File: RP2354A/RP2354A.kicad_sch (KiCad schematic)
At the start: 22 parts, among them J101 USB4085-GF-A, J102 AudioJack2_SwitchT, J103 AudioJack2_SwitchT, Q101 MMBF5103

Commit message: First cut at BOM selection for caps and resistors
The size choices were a bit random, this standardizes on 0402 for
resistors.  Also, optimize the BOM by just sharing values where they
don't matter that much.

For example, we need those 5k1 resistors for the USB CC pulldowns, and
we might as well then use that for the i2c pullup resistors too.  And
the self-biasing source resistor for the JFET input could use the same.

For similar reasons, just standardize on 33R for the low value resistors
that we use for the USB data line serial termination and the analog
voltage RC filtering.

Capacitors are 0402 for small values (0.1uF and smaller) or 0603 for
bigger capacitance values.  That seems to match availability.

Signed-off-by: Linus Torvalds <torvalds@linux-foundation.org>
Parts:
- C101, C103, C105, C106, C107: footprint Capacitor_SMD:C_1206_3216Metric -> Capacitor_SMD:C_0603_1608Metric
- C102, C104: footprint Capacitor_SMD:C_0805_2012Metric -> Capacitor_SMD:C_0402_1005Metric
- R106, R107: value 3k3 -> 5k1
- R110: value 100R -> 33R
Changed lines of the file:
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@@
 			)
 		)
-		(property "Footprint" "Capacitor_SMD:C_1206_3216Metric"
+		(property "Footprint" "Capacitor_SMD:C_0603_1608Metric"
 			(at 43.18 118.4148 0)
 			(effects
@@
 			)
 		)
-		(property "Footprint" "Capacitor_SMD:C_0805_2012Metric"
+		(property "Footprint" "Capacitor_SMD:C_0402_1005Metric"
 			(at 154.6352 99.06 0)
 			(effects
@@
 			)
 		)
-		(property "Footprint" "Capacitor_SMD:C_0805_2012Metric"
+		(property "Footprint" "Capacitor_SMD:C_0402_1005Metric"
 			(at 58.7248 130.81 0)
 			(effects
@@
 			)
 		)
-		(property "Footprint" "Capacitor_SMD:C_1206_3216Metric"
+		(property "Footprint" "Capacitor_SMD:C_0603_1608Metric"
 			(at 165.4048 41.91 0)
 			(effects
@@
 			)
 		)
-		(property "Value" "100R"
+		(property "Value" "33R"
 			(at 176.53 34.29 90)
 			(effects
@@
 			)
 		)
-		(property "Value" "3k3"
+		(property "Value" "5k1"
 			(at 83.82 132.08 0)
 			(effects
@@
 			)
 		)
-		(property "Footprint" "Capacitor_SMD:C_1206_3216Metric"
+		(property "Footprint" "Capacitor_SMD:C_0603_1608Metric"
 			(at 100.33 125.4252 0)
 			(effects
@@
 			)
 		)
-		(property "Footprint" "Capacitor_SMD:C_1206_3216Metric"
+		(property "Footprint" "Capacitor_SMD:C_0603_1608Metric"
 			(at 167.64 93.0148 0)
 			(effects
@@
 			)
 		)
-		(property "Value" "3k3"
+		(property "Value" "5k1"
 			(at 88.9 43.18 0)
 			(effects
@@
 			)
 		)
-		(property "Footprint" "Capacitor_SMD:C_1206_3216Metric"
+		(property "Footprint" "Capacitor_SMD:C_0603_1608Metric"
 			(at 185.7248 41.91 0)
 			(effects

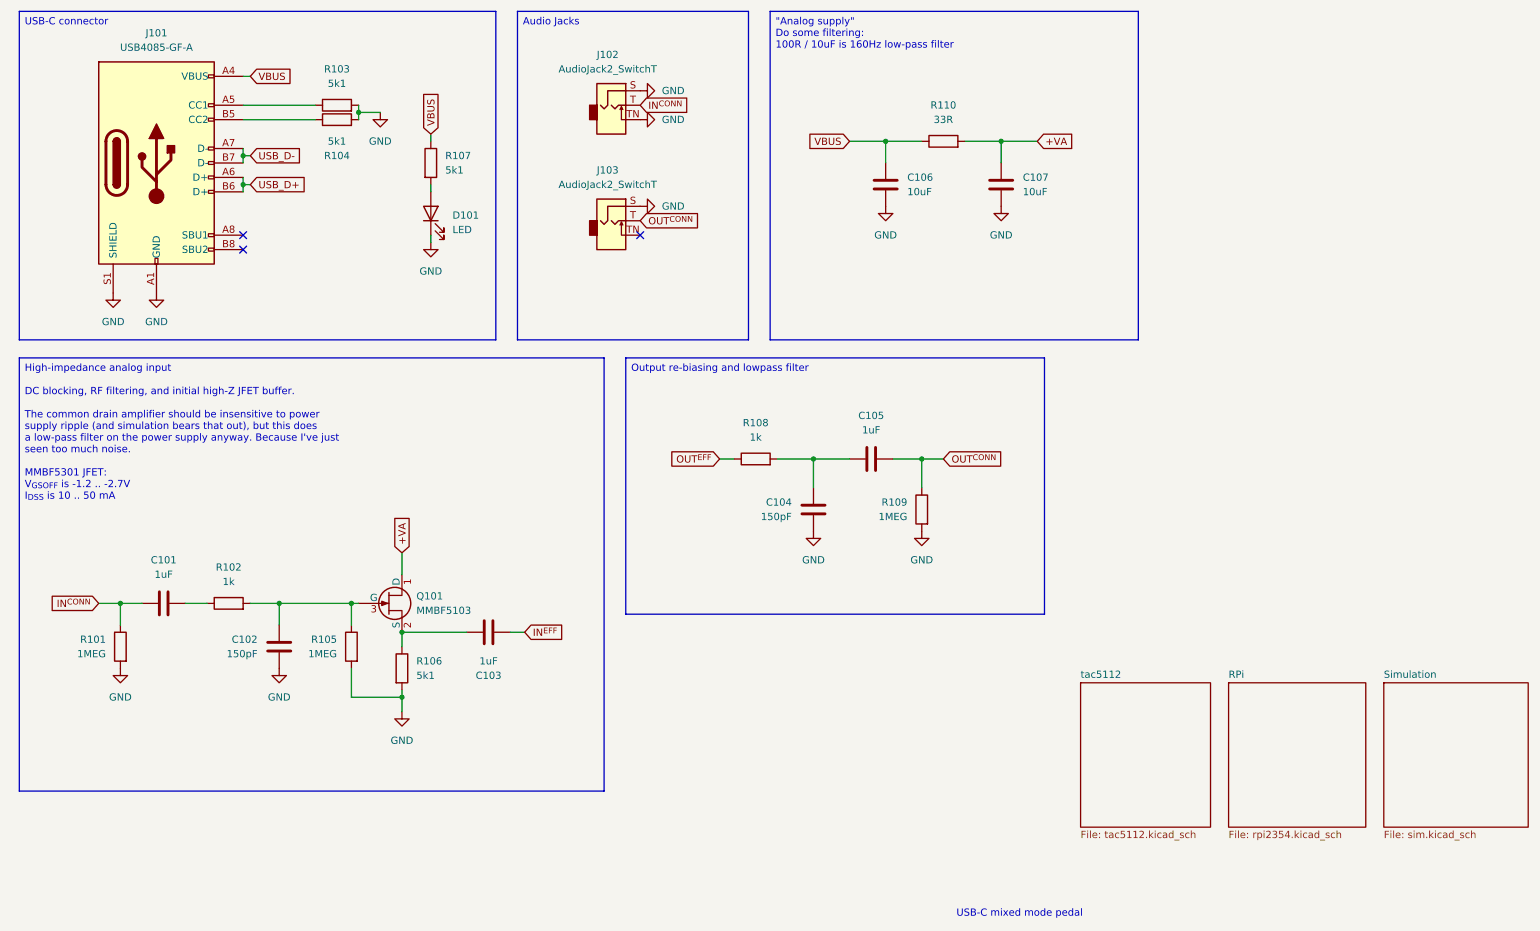
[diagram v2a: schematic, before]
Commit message: Switch the MMBF5103 JFET over to a OPA365 op amp
This is a long time coming, but it was triggered by jlcpcb not stocking
the MMBF5103, and all the alternatives looked worse.  So I guess sanity
has to prevail, and I should use an opamp rather than a discrete JFET
input stage.

I looked at the J201 - which I have tested and works, but has a
potentially very low V_{GSOFF} that will cause clipping.  And the
MMBFJ309L looked good in simulation and had better parameter values, but
I've never tested it, so it seemed a bit risky particularly since the
intended market seems to be for much higher frequency circuits.

I even looked at the JFE150, which is another silly-expensive thing sold
to audio markets.  I guess that tracks.

In the end, a plain simple opamp is definitely the sane choice.

To rebias the incoming signal, this uses the MICBIAS from the TAC5112,
which is typically 2.75V (but can be programmed to 2.5V or turned off
entirely etc).  It's there, it's almost what it is meant for, so let's
use it.

The OPA365 looks fine, and does rail-to-rail input and output and can do
single supplies down to 2.2V, but rather than put even more on the 3.3V
rail (and limiting the voltage swing), this just uses the 5V USB VBUS
power supply.

This does have some minimal caps for filtering (replacing the old +VA
supply to the JFET) but the OPA365 also claims good PSRR.

This all does seem like the right thing to do, but I'm still a bit sad
since the discrete JFET was just more interesting.

Signed-off-by: Linus Torvalds <torvalds@linux-foundation.org>
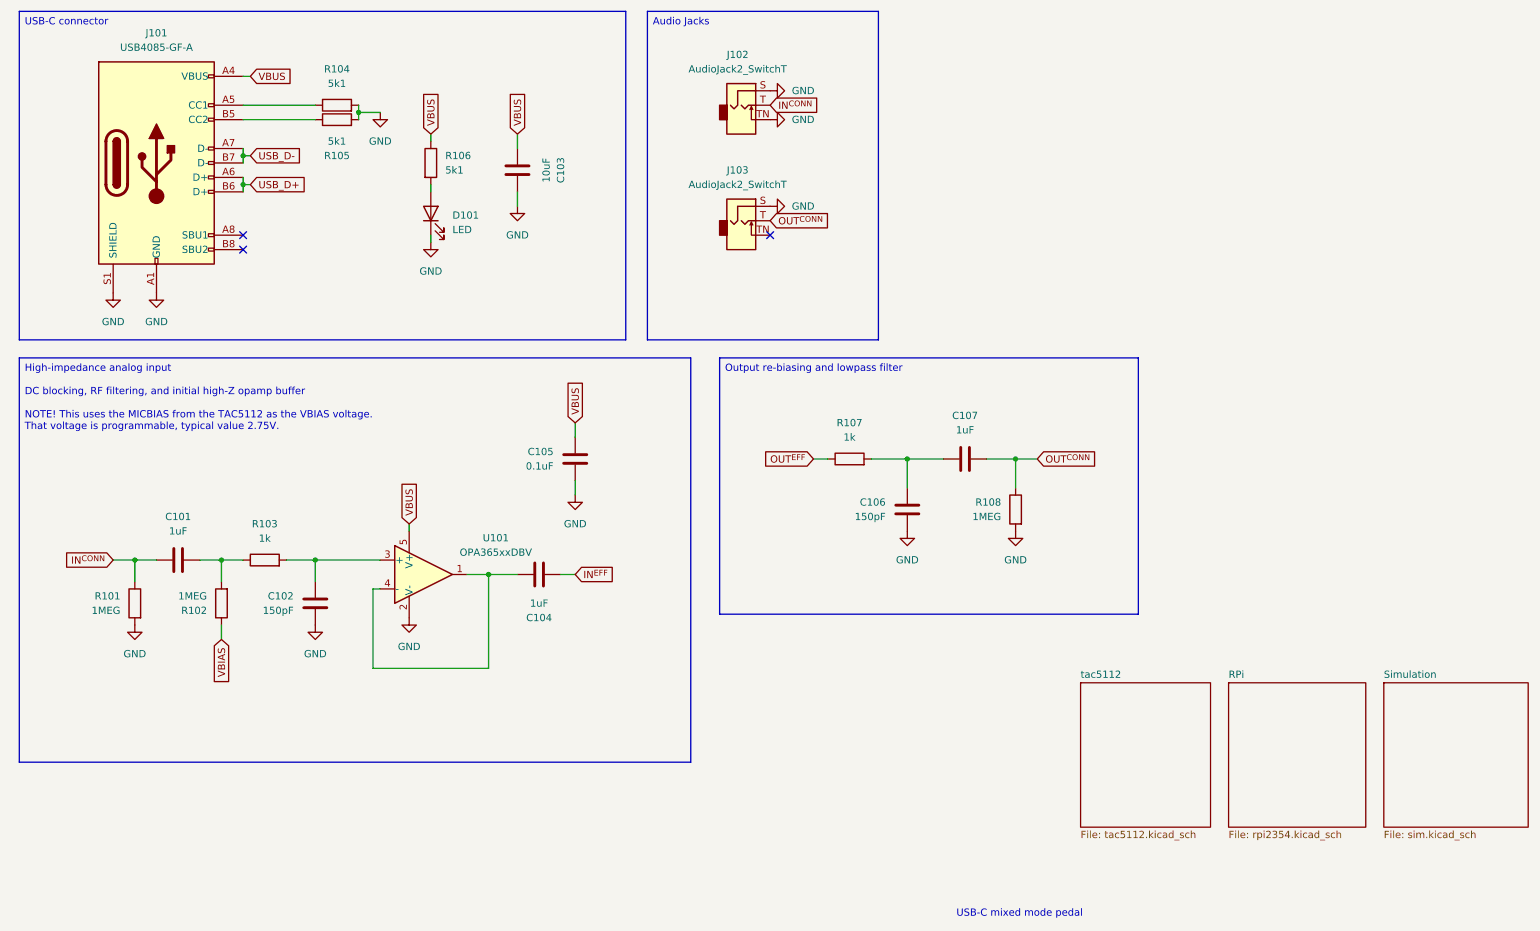
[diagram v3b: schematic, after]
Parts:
- removed C106, C107: 10uF, Capacitor_SMD:C_0603_1608Metric, symbol Device:C
- removed Q101: MMBF5103, Package_TO_SOT_SMD:SOT-23, symbol Mylib:MMBF5103
- removed R105: 1MEG, Resistor_SMD:R_0402_1005Metric, symbol Device:R
- removed R106: 5k1, Resistor_SMD:R_0402_1005Metric, symbol Device:R
- removed R110: 33R, Resistor_SMD:R_0402_1005Metric, symbol Device:R
- added C103: 10uF, Capacitor_SMD:C_0603_1608Metric, symbol Device:C
- added C105: 0.1uF, Capacitor_SMD:C_0402_1005Metric, symbol Device:C
- added R102: 1MEG, Resistor_SMD:R_0402_1005Metric, symbol Device:R
- added U101: OPA365xxDBV, Package_TO_SOT_SMD:SOT-23-5, symbol Amplifier_Operational:OPA365xxDBV
- renumbered C103 to C104, C104 to C106, C105 to C107, R102 to R103, R103 to R104, R104 to R105, R107 to R106, R108 to R107, R109 to R108
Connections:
- net GND: now also C103.1, C105.1, U101.2 (V-)
- net VBUS: now also C103.2, C105.2, U101.5 (V+)
- net at C101.2, R103.1: now also R102.2
- net at C104.1: now also U101.1, U101.4 (-)
- net at C102.1, R103.2: now also U101.3 (+)
- new net VBIAS: R102.1
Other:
- moved on the sheet: C101, C102, C104, C106, C107, J102, J103, R101, R103, R107, R108

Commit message: rp2354: First stab at pcb layout
This is an insane 6-layer stackup, not because I need six layers
(although it does allow me to be even lazier than usual), but because I
want to use via-in-pad and at that point jlcpcb pretty much ends up
doing the whole precision 6-layer thing anyway.

The minimal RP2354A board makes do with just a simple two-layer stackup,
and I'm sure this could have been done that way too.  But with four
layers it's easy to just use one layer for the +1V1 zone and one for the
+3V3 zone under the RP2354A, and just bring things in with the vias.

This is all connected, but with some ERC noise. Mostly harmless (tm).

Also add JLCPCB part numbers to things, although I need to check them
all several times.

Signed-off-by: Linus Torvalds <torvalds@linux-foundation.org>
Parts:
- added C8, C9: 10uF, Capacitor_SMD:C_0603_1608Metric, symbol Device:C
- added U2: NCP1117-3.3_SOT223, Package_TO_SOT_SMD:SOT-223-3_TabPin2, symbol Regulator_Linear:NCP1117-3.3_SOT223
- C1: renamed from C101; JLCPCB (none) -> C519560
- C2: renamed from C102; JLCPCB (none) -> C710836
- C3: renamed from C103; JLCPCB (none) -> C91606
- C4: renamed from C104; JLCPCB (none) -> C519560
- C5: renamed from C105; JLCPCB (none) -> C1525
- C6: renamed from C106; JLCPCB (none) -> C710836
- C7: renamed from C107; JLCPCB (none) -> C519560
- D1: renamed from D101; JLCPCB (none) -> C160479
- J1: renamed from J101; value USB4085-GF-A -> TYPE-C16PIN; JLCPCB (none) -> C393939
- J2: renamed from J102; now not fitted
- J3: renamed from J103; now not fitted
- R1: renamed from R101; JLCPCB (none) -> C26083
- R2: renamed from R102; JLCPCB (none) -> C26083
- R3: renamed from R103; JLCPCB (none) -> C11702
- R4: renamed from R104; JLCPCB (none) -> C25905
- R5: renamed from R105; JLCPCB (none) -> C25905
- R6: renamed from R107; JLCPCB (none) -> C11702
- R7: renamed from R108; JLCPCB (none) -> C26083
- R8: renamed from R106; value 5k1 -> 1k; JLCPCB (none) -> C11702
- U1: renamed from U101; JLCPCB (none) -> C96626
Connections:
- net GND: now also C8.2, C9.2, U2.1 (GND)
- net VBUS: now also C8.1, U2.3 (VI); no longer R8.1
- new net +3V3: C9.1, R8.1, U2.2 (VO)
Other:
- moved on the sheet: D1, R8

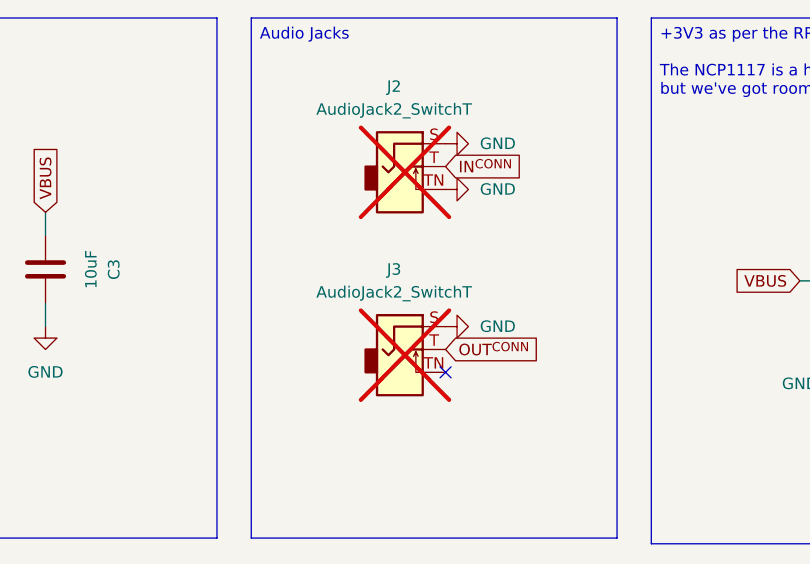
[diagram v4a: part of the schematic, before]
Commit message: Fix missing JLCPCB number, and replace "DNP" with "not in BOM"
Also cross-verify the JLCPCB numbers.

Signed-off-by: Linus Torvalds <torvalds@linux-foundation.org>
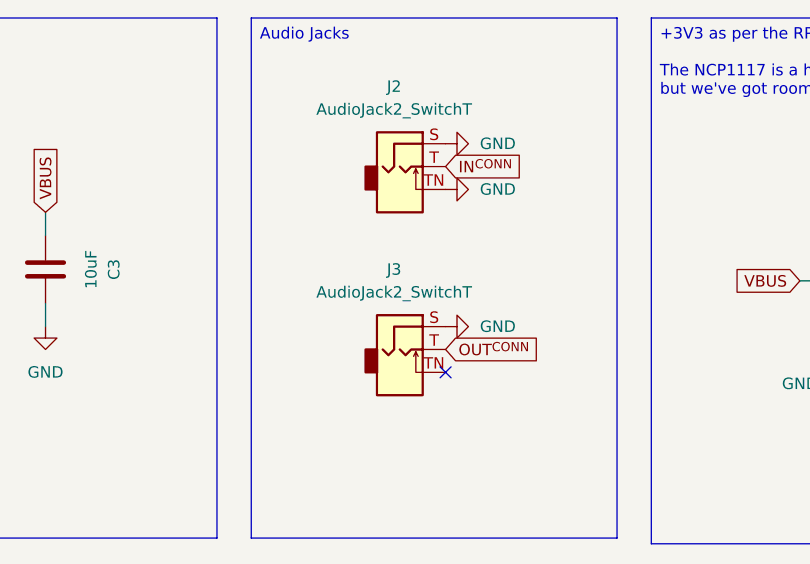
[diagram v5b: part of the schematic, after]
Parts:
- J2, J3: now fitted; now left out of the parts list
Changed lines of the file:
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@@
 		(unit 1)
 		(exclude_from_sim yes)
-		(in_bom yes)
-		(on_board yes)
-		(dnp yes)
+		(in_bom no)
+		(on_board yes)
+		(dnp no)
 		(fields_autoplaced yes)
 		(property "Reference" "J2"
@@
 		(unit 1)
 		(exclude_from_sim yes)
-		(in_bom yes)
-		(on_board yes)
-		(dnp yes)
+		(in_bom no)
+		(on_board yes)
+		(dnp no)
 		(fields_autoplaced yes)
 		(property "Reference" "J3"

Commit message: Rename the "JLCPCB" property as "LCSC PN"
That's apparently the standard way for the 'JLCPCB Fabrication Toolkit'
scripting.  At least for the first time, I want to cross-check with the
scripting, even if I might not necessarily use it as-is.

Signed-off-by: Linus Torvalds <torvalds@linux-foundation.org>
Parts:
- C1, C4, C7: JLCPCB C519560 -> (none); LCSC PN (none) -> C519560
- C2, C6: JLCPCB C710836 -> (none); LCSC PN (none) -> C710836
- C3, C8, C9: JLCPCB C91606 -> (none); LCSC PN (none) -> C91606
- C5: JLCPCB C1525 -> (none); LCSC PN (none) -> C1525
- D1: JLCPCB C160479 -> (none); LCSC PN (none) -> C160479
- J1: JLCPCB C393939 -> (none); LCSC PN (none) -> C393939
- R1, R2, R7: JLCPCB C26083 -> (none); LCSC PN (none) -> C26083
- R3, R6, R8: JLCPCB C11702 -> (none); LCSC PN (none) -> C11702
- R4, R5: JLCPCB C25905 -> (none); LCSC PN (none) -> C25905
- U1: JLCPCB C96626 -> (none); LCSC PN (none) -> C96626
- U2: JLCPCB C26537 -> (none); LCSC PN (none) -> C26537
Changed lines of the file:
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@@
 			)
 		)
-		(property "JLCPCB" "C26537"
+		(property "LCSC PN" "C26537"
 			(at 207.01 44.45 0)
 			(effects
@@
 			)
 		)
-		(property "JLCPCB" "C91606"
+		(property "LCSC PN" "C91606"
 			(at 189.23 49.53 0)
 			(effects
@@
 			)
 		)
-		(property "JLCPCB" "C91606"
+		(property "LCSC PN" "C91606"
 			(at 224.79 49.53 0)
 			(effects
@@
 			)
 		)
-		(property "JLCPCB" "C519560"
+		(property "LCSC PN" "C519560"
 			(at 41.91 111.76 90)
 			(effects
@@
 			)
 		)
-		(property "JLCPCB" "C710836"
+		(property "LCSC PN" "C710836"
 			(at 170.18 102.87 0)
 			(effects
@@
 			)
 		)
-		(property "JLCPCB" "C91606"
+		(property "LCSC PN" "C91606"
 			(at 101.6 43.18 90)
 			(effects
@@
 			)
 		)
-		(property "JLCPCB" "C11702"
+		(property "LCSC PN" "C11702"
 			(at 57.15 111.76 90)
 			(effects
@@
 			)
 		)
-		(property "JLCPCB" "C25905"
+		(property "LCSC PN" "C25905"
 			(at 69.85 34.29 90)
 			(effects
@@
 			)
 		)
-		(property "JLCPCB" "C710836"
+		(property "LCSC PN" "C710836"
 			(at 66.04 119.38 0)
 			(effects
@@
 			)
 		)
-		(property "JLCPCB" "C26083"
+		(property "LCSC PN" "C26083"
 			(at 189.23 102.87 0)
 			(effects
@@
 			)
 		)
-		(property "JLCPCB" "C25905"
+		(property "LCSC PN" "C25905"
 			(at 69.85 31.75 90)
 			(effects
@@
 			)
 		)
-		(property "JLCPCB" "C11702"
+		(property "LCSC PN" "C11702"
 			(at 160.02 93.98 90)
 			(effects
@@
 			)
 		)
-		(property "JLCPCB" "C160479"
+		(property "LCSC PN" "C160479"
 			(at 251.46 45.72 90)
 			(effects
@@
 			)
 		)
-		(property "JLCPCB" ""
+		(property "LCSC PN" ""
 			(at 140.97 31.75 0)
 			(effects
@@
 			)
 		)
-		(property "JLCPCB" "C519560"
+		(property "LCSC PN" "C519560"
 			(at 105.41 114.3 90)
 			(effects
@@
 			)
 		)
-		(property "JLCPCB" "C96626"
+		(property "LCSC PN" "C96626"
 			(at 85.09 114.3 0)
 			(effects
@@
 			)
 		)
-		(property "JLCPCB" "C393939"
+		(property "LCSC PN" "C393939"
 			(at 38.1 41.91 0)
 			(effects
@@
 			)
 		)
-		(property "JLCPCB" ""
+		(property "LCSC PN" ""
 			(at 140.97 52.07 0)
 			(effects
@@
 			)
 		)
-		(property "JLCPCB" "C519560"
+		(property "LCSC PN" "C519560"
 			(at 180.34 93.98 90)
 			(effects
@@
 			)
 		)
-		(property "JLCPCB" "C11702"
+		(property "LCSC PN" "C11702"
 			(at 251.46 36.83 0)
 			(effects
@@
 			)
 		)
-		(property "JLCPCB" "C1525"
+		(property "LCSC PN" "C1525"
 			(at 111.76 93.98 0)
 			(effects
@@
 			)
 		)
-		(property "JLCPCB" "C26083"
+		(property "LCSC PN" "C26083"
 			(at 34.29 119.38 0)
 			(effects
@@
 			)
 		)
-		(property "JLCPCB" "C26083"
+		(property "LCSC PN" "C26083"
 			(at 49.53 119.38 0)
 			(effects
